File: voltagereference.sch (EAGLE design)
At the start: 48 parts, among them J1 KOBICONN_163-179PH-EX, U1 MAX6341, U2 TI_LM2937

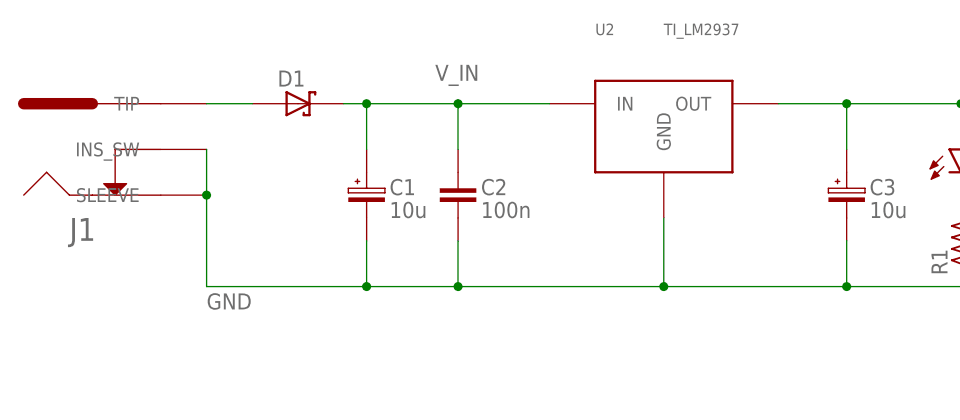
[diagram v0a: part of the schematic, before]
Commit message: Added pdfs, modified schematic
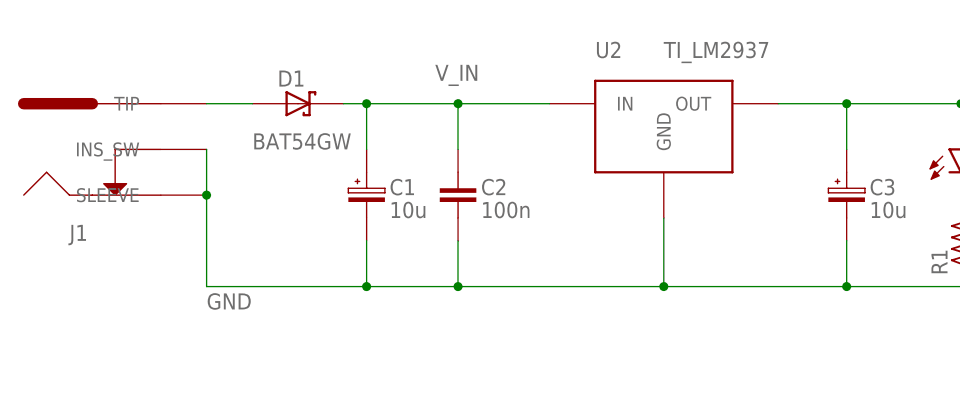
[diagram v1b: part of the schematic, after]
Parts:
- D1: value NEX_BAT54GW -> BAT54GW
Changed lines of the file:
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@@
 <part name="C2" library="travis" deviceset="C_0805" device="" value="100n"/>
 <part name="C3" library="travis" deviceset="PANASONIC_EEE_4MM" device="" value="10u"/>
-<part name="D1" library="travis" deviceset="NEX_BAT54GW" device=""/>
+<part name="D1" library="travis" deviceset="NEX_BAT54GW" device="" value="BAT54GW"/>
 <part name="U2" library="travis" deviceset="TI_LM2937" device=""/>
 <part name="R1" library="travis" deviceset="R_0805" device="" value="1k"/>
@@
 <instances>
 <instance part="J1" gate="G$1" x="20.32" y="106.68" smashed="yes">
-<attribute name="NAME" x="15.24" y="96.52" size="2.54" layer="95"/>
+<attribute name="NAME" x="15.24" y="96.52" size="1.778" layer="95"/>
 </instance>
 <instance part="C1" gate="G$1" x="48.26" y="101.6" smashed="yes">
@@
 <instance part="D1" gate="G$1" x="40.64" y="111.76" smashed="yes">
 <attribute name="NAME" x="38.354" y="113.665" size="1.778" layer="95"/>
+<attribute name="VALUE" x="35.56" y="106.68" size="1.778" layer="96"/>
 </instance>
 <instance part="U2" gate="G$1" x="81.28" y="109.22" smashed="yes">
-<attribute name="NAME" x="73.66" y="119.38" size="1.27" layer="95"/>
-<attribute name="VALUE" x="81.28" y="119.38" size="1.27" layer="96"/>
+<attribute name="NAME" x="73.66" y="116.84" size="1.778" layer="95"/>
+<attribute name="VALUE" x="81.28" y="116.84" size="1.778" layer="96"/>
 </instance>
 <instance part="R1" gate="G$1" x="114.3" y="96.52" smashed="yes" rot="R90">
